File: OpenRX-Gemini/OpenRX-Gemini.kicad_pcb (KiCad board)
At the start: 6 copper layers, 17 x 17.6 mm, 85 parts, among them J1 Conn_Coaxial_Small, J2 Conn_Coaxial_Small, T1 0900PC16J0042001E, T2 0900PC16J0042001E, U1 ESP32-C3, U2 TLV75533PDQNR, U3 LR1121IMLTRT, U4 RFX2401C, U5 SKY13373-460LF, U6 LR1121IMLTRT, U7 RFX2401C, U8 SKY13373-460LF, U9 TS2306A 240GF MSM 9_C2976675, X1 CJ17-400001010B20

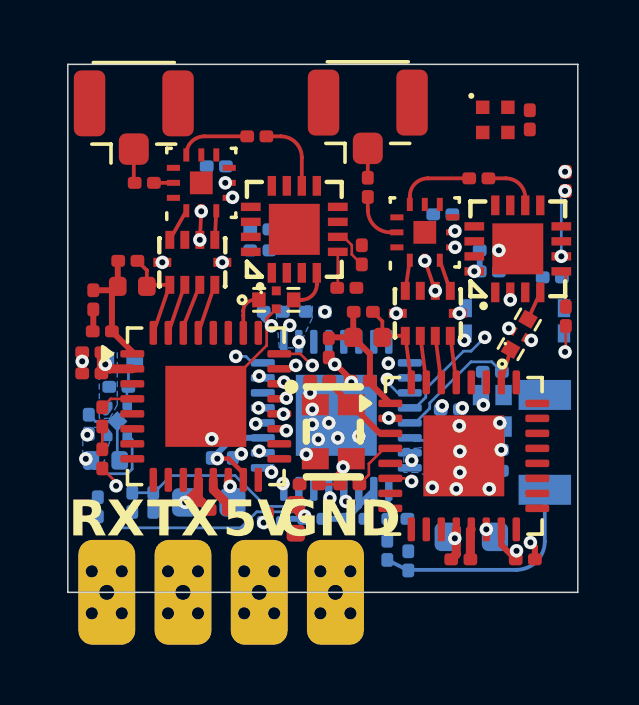
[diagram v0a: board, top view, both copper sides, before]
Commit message: add via testing board
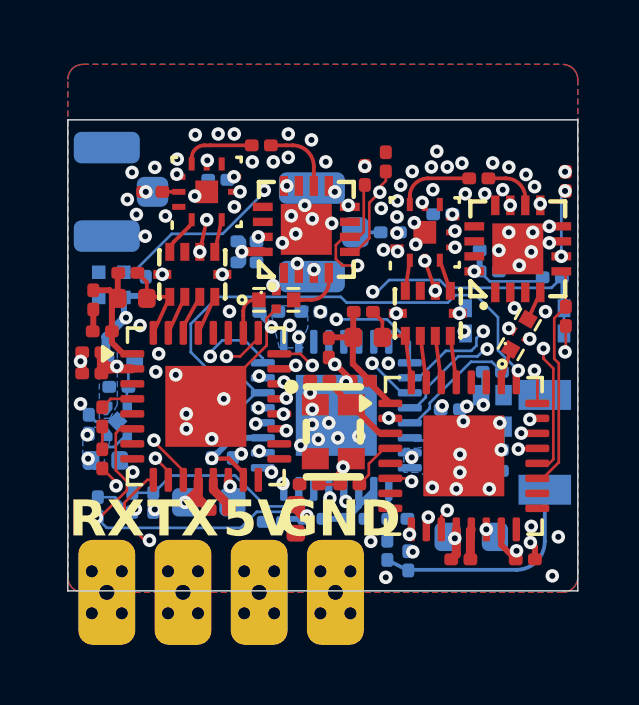
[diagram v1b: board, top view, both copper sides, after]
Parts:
- C12, C44, D1, J1, J2: moved to B.Cu
- moved C12 14.0 mm to (102.6, 106.8), turned to 90 degrees
- moved D1 13.9 mm to (101.5, 106.8)
- moved J2 4.71 mm to (108.1, 105.0), turned to 180 degrees
- moved R7 4.40 mm to (110.6, 102.7), turned to -90 degrees
- moved J1 3.08 mm to (101.3, 103.7), turned to 180 degrees
- moved R8 2.65 mm to (109.9, 103.1)
- moved C44 1.68 mm to (110.8, 105.0), turned to 180 degrees
- moved C21 0.59 mm to (106.0, 106.0)
- moved C31 0.59 mm to (106.0, 105.3)
- moved C22 0.45 mm to (105.0, 103.2)
- moved C24 0.41 mm to (102.8, 103.7)
- moved L5 0.40 mm to (102.2, 107.2)
- moved T1 0.40 mm to (104.2, 106.4)
- moved U4 0.40 mm to (108.0, 104.9)
- moved R1 0.40 mm to (102.0, 106.3)
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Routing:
- net Net-(U1-U0TXD): track 3.64 -> 34.7 mm
- net /ESP32-C3/LED: track 0.00 -> 23.5 mm, vias 0 -> 3
- net Net-(U1-U0RXD): track 0.99 -> 22.0 mm, vias 1 -> 2
- net /ESP32-C3/DIO1_B: track 0.00 -> 19.6 mm, vias 0 -> 2
- net /ESP32-C3/BUSY_B: track 0.25 -> 18.9 mm, vias 0 -> 1
- net /LR1121_A/TXEN24: track 1.76 -> 19.8 mm, vias 1 -> 2
- net +3V3: track 13.0 -> 28.9 mm, vias 11 -> 18
- net /LR1121_B/CTRL2: track 0.09 -> 14.9 mm, vias 1 -> 2
- net /ESP32-C3/RST_B: track 1.74 -> 16.4 mm
- net /ESP32-C3/BOOT: track 0.15 -> 14.8 mm, vias 1 -> 2
- net /ESP32-C3/MOSI: track 0.53 -> 15.0 mm, vias 2 -> 3
- net /LR1121_A/CTRL2: track 0.13 -> 14.4 mm, vias 1 -> 2
- net /ESP32-C3/MISO: track 0.39 -> 13.4 mm, vias 2 -> 3
- net /LR1121_B/CTRL1: track 0.08 -> 12.8 mm, vias 1 -> 2
- net /LR1121_A/CTRL1: track 0.12 -> 12.8 mm, vias 1 -> 2
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- added copper zone on In3.Cu, net +3V3
- added copper zone on B.Cu, net GND
- added copper zone on F.Cu, net GND
- added copper zone on In1.Cu, net GND
- added copper zone on In2.Cu, net GND
- added copper zone on In3.Cu, net GND
- added copper zone on In4.Cu, net GND
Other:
- board size 17 x 17.6 mm -> 17 x 15.7 mm
